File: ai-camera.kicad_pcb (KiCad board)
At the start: 4 copper layers, 70 x 70 mm, 188 parts, among them J1 Conn-01x02_P2mm_S2B-PH-K-S_Ho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, J2 USB_B_Micro_10118194-0001LF, J3 DBG, J4 Conn-02x10_P2.54mm_B-2100S20P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, J5 Conn-01x02_P1.25mm_10114829-1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, J6 Conn_01x24_FFC_0.5mm_hirose_F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, J7 Conn_01x24_FFC_0.5mm_hirose_F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, Q1 AO3401A, Q10 AO3401A, Q2 AO3400A, Q3 AO3400A, Q4 AO3400A, Q5 AO3401A, Q6 AO3400A, Q7 AO3401A, Q8 AO3400A, Q9 AO3400A, SW1 SW_PB_TS-1187A-B-A-B, SW2 SW_PB_TS-1187A-B-A-B, SW3 SW_PB_TS-1187A-B-A-B, SW4 SW_PB_TS-1187A-B-A-B, U1 SRV05-4, U10 RT9166-12GVL, U11 ESP32-S3-WROOM-1-N16R8, U12 MT9284-28J, U2 TP4057-42-SOT26-R, U3 PCF8563T/5,518, U4 XC6206-2.8V, U5 PIR_BS612, U6 SY8089AAAC, U7 SOT-23-6_SN74LVC1G373DBVR_TI, U8 AP1511B, U9 XC6206-2.8V, Y1 32.768kHz_Q13FC1350000400

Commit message: ai camera layout: begin
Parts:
- removed the C24 at (220.1, 92.6)
- removed the C29 at (230.4, 81.7)
- removed the Q4 at (247.4, 74.5)
- removed the R17 at (265.5, 72.6)
- removed the R20 at (265.9, 74.5)
- removed the R23 at (288.8, 51.1)
- removed the R24 at (259.5, 79.1)
- removed the R27 at (250.0, 88.3)
- removed the R34 at (273.3, 66.4)
- removed the R38 at (263.0, 77.5)
- removed the R39 at (279.3, 61.1)
- added C26: 1u_1206_CL31B105KCHNNNE, Capacitor_SMD:C_1206_3216Metric, F.Cu at (309.3, 32.7)
- added C28: 1u_1206_CL31B105KCHNNNE, Capacitor_SMD:C_1206_3216Metric, F.Cu at (315.1, 29.3)
- added C30: 100n_0402_CL05B104KB54PNC, Capacitor_SMD:C_0402_1005Metric, F.Cu at (307.9, 41.3)
- added C34: 1u_1206_CL31B105KCHNNNE, Capacitor_SMD:C_1206_3216Metric, F.Cu at (298.0, 36.0)
- added D5: B5819W-SL_SOD-123, Diode_SMD:D_SOD-123, F.Cu at (298.1, 29.3)
- added R18: 215k_0402_0402WGD2153TCE, Resistor_SMD:R_0402_1005Metric, F.Cu at (307.9, 39.3)
- added R21: 215k_0402_0402WGD2153TCE, Resistor_SMD:R_0402_1005Metric, F.Cu at (307.9, 35.4)
- added R25: 215k_0402_0402WGD2153TCE, Resistor_SMD:R_0402_1005Metric, F.Cu at (310.9, 38.0)
- added R32: 215k_0402_0402WGD2153TCE, Resistor_SMD:R_0402_1005Metric, F.Cu at (313.6, 34.0)
- added R33: 215k_0402_0402WGD2153TCE, Resistor_SMD:R_0402_1005Metric, F.Cu at (316.5, 32.0)
- added R36: 215k_0402_0402WGD2153TCE, Resistor_SMD:R_0402_1005Metric, F.Cu at (313.6, 32.0)
- C13, C19, C20, C21, C4, C6: value 22u_1206_CL31A226KOHNNNE -> 1u_1206_CL31B105KCHNNNE
- C27: value 100n_0402_CL05B104KB54PNC -> 22u_1206_CL31A226KOHNNNE; footprint Capacitor_SMD:C_0402_1005Metric -> Capacitor_SMD:C_1206_3216Metric
- R16, R19, R22, R37: value 10k_0402_0402WGF1002TCE -> 215k_0402_0402WGD2153TCE
- moved L1 174.6 mm to (102.3, 67.5)
- moved R6 172.4 mm to (171.9, 154.5)
- moved C3 170.4 mm to (101.2, 85.0), turned to 180 degrees
- moved R9 156.9 mm to (163.8, 129.5)
- moved R15 155.5 mm to (151.1, 131.2), turned to 90 degrees
- moved U2 139.7 mm to (160.7, 130.0)
- moved H3 133.6 mm to (279.8, 104.6)
- moved J4 133.6 mm to (269.2, 118.1)
- moved J5 133.6 mm to (282.0, 140.1)
- moved SW2 133.6 mm to (275.1, 145.6)
- moved H1 133.6 mm to (279.1, 162.2)
- moved J6 133.6 mm to (234.8, 137.0)
- moved J7 133.6 mm to (264.7, 102.5)
- moved L2 133.6 mm to (231.8, 156.5)
- moved L3 133.6 mm to (246.6, 156.5)
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- renumbered C16 to C15, C17 to C16, C15 to C17, C22 to C18, C23 to C22, C18 to C23, C25 to C24, C26 to C25, C28 to C29, C30 to C31, C31 to C32, C32 to C33, C33 to C35, C34 to C36, C35 to C37, C36 to C38, D5 to D6, D6 to D7, Q5 to Q4, Q6 to Q5, Q7 to Q6, Q8 to Q7, Q9 to Q8, Q10 to Q9, R3 to R1, R18 to R17, R4 to R2, R21 to R20, R25 to R23, R26 to R24, R28 to R26, R29 to R27, R30 to R28, R31 to R29, R5 to R3, R32 to R30, R33 to R31, R35 to R34, R36 to R35, R40 to R38, R41 to R39, R6 to R4, R42 to R40, R7 to R5, R1 to R6, R2 to R7
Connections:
- C18 pad 1: +3V3 -> GND
- C18 pad 2: GND -> +3V3
- C19 pad 1: Net-(C19-Pad1) -> GND
- C19 pad 2: GND -> +3V3
- C20 pad 1: Net-(C19-Pad1) -> Net-(Q9-Pad3)
- C21 pad 1: +3V3 -> Net-(Q9-Pad3)
- C22 pad 1: +3V3 -> GND
- C22 pad 2: GND -> +3V3
- C27 pad 1: +3V3 -> GND
- C27 pad 2: GND -> VBUS
- C4 pad 1: VBUS -> GND
- C4 pad 2: GND -> VBUS
- C6 pad 1: Net-(C6-Pad1) -> Net-(Q1-Pad1)
- C6 pad 2: Net-(C6-Pad2) -> Net-(Q1-Pad2)
- J4 pad 19: /IO40 -> GND
- JP1 pad 1: Net-(D1-Pad1) -> Net-(JP1-Pad1)
- JP1 pad 2: VBUS -> Net-(D1-Pad1)
- Q1 pad 1: Net-(C6-Pad2) -> Net-(Q1-Pad1)
- Q1 pad 2: Net-(C6-Pad1) -> Net-(Q1-Pad2)
- Q4 pad 1: Net-(C6-Pad2) -> Net-(Q1-Pad1)
- Q4 pad 2: Net-(C6-Pad1) -> Net-(Q1-Pad2)
- Q5 pad 3: Net-(Q6-Pad3) -> Net-(Q5-Pad3)
- Q6 pad 1: Net-(Q6-Pad3) -> Net-(Q5-Pad3)
- Q6 pad 3: Net-(Q7-Pad3) -> Net-(Q6-Pad3)
- Q7 pad 3: Net-(Q6-Pad3) -> Net-(Q5-Pad3)
- Q8 pad 1: /PWR_EN -> /CAM_PWR_EN
- Q9 pad 3: Net-(C19-Pad1) -> Net-(Q9-Pad3)
- R12 pad 1: Net-(C6-Pad2) -> Net-(Q1-Pad1)
- R12 pad 2: Net-(C6-Pad1) -> Net-(Q1-Pad2)
- R15 pad 1: Net-(Q4-Pad3) -> Net-(JP1-Pad1)
- R15 pad 2: Net-(C6-Pad2) -> Net-(Q1-Pad1)
- R16 pad 2: Net-(D1-Pad1) -> Net-(JP2-Pad2)
- R19 pad 1: Net-(Q6-Pad3) -> GND
- R19 pad 2: VBUS -> /PWR_EN
- R22 pad 2: Net-(Q7-Pad3) -> /PIR_CTRL_LE
- R37 pad 1: /IRCUT_CTRL -> /CAM.PWDN
- R6 pad 1: +5P -> Net-(D1-Pad1)
- SW1 pad 1: Net-(Q6-Pad3) -> Net-(Q5-Pad3)
- TP17 pad 1: /IO40 -> /CAM_PWR_EN
- U1 pad 5: +5F -> Net-(J2-Pad1)
- U10 pad 3: Net-(C19-Pad1) -> Net-(Q9-Pad3)
- U11 pad 33: /IO40 -> /CAM_PWR_EN
- U3 pad 3: Net-(Q6-Pad3) -> Net-(Q5-Pad3)
- U6 pad 1: Net-(Q7-Pad3) -> Net-(Q6-Pad3)
- U9 pad 3: Net-(C19-Pad1) -> Net-(Q9-Pad3)

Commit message: ai camera review 8: replace 1u/1206 with 10u/0603
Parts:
- removed the C17 at (214.4, 92.6)
- removed Q8: AO3400A, Package_TO_SOT_SMD:SOT-23
- removed Q9: AO3401A, Package_TO_SOT_SMD:SOT-23
- removed the R15 at (151.1, 131.2)
- removed the R33 at (316.5, 32.0)
- removed the R34 at (295.1, 46.0)
- removed the R35 at (280.3, 59.1)
- removed R37: 215k_0402_0402WGD2153TCE, Resistor_SMD:R_0402_1005Metric
- removed the TP10 at (255.1, 73.5)
- removed the TP11 at (234.8, 90.7)
- removed the TP12 at (292.1, 42.8)
- removed the TP9 at (229.5, 96.9)
- added C1: 1u_1206_CL31B105KCHNNNE, Capacitor_SMD:C_1206_3216Metric, F.Cu at (238.5, 90.5)
- added C8: 100n_0402_CL05B104KB54PNC, Capacitor_SMD:C_0402_1005Metric, F.Cu at (242.8, 91.8)
- added R12: 215k_0402_0402WGD2153TCE, Resistor_SMD:R_0402_1005Metric, F.Cu at (242.8, 89.8)
- moved L1 89.6 mm to (110.3, 156.7)
- moved C4 89.6 mm to (109.2, 174.2)
- moved D1 89.6 mm to (118.8, 168.8)
- moved J1 89.6 mm to (109.7, 168.5)
- moved U1 89.6 mm to (110.1, 160.0)
- moved D2 89.6 mm to (121.1, 168.8)
- moved J2 89.6 mm to (105.7, 160.2)
- moved TP30 78.7 mm to (319.6, 100.8)
- moved TP49 75.9 mm to (313.0, 101.6)
- moved R18 74.8 mm to (225.2, 50.4)
- moved C16 74.8 mm to (224.0, 54.4)
- moved C21 74.8 mm to (228.1, 50.4)
- moved C39 74.8 mm to (224.0, 52.4)
- moved R14 74.8 mm to (228.1, 48.4)
- moved R32 74.5 mm to (239.4, 40.9)
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- renumbered C8 to C10, C9 to C11, C10 to C12, C11 to C13, C12 to C14, C13 to C15, C14 to C16, C15 to C17, C16 to C18, C20 to C19, C1 to C2, C21 to C20, C18 to C21, C19 to C22, C24 to C23, C25 to C24, C22 to C25, C23 to C26, C26 to C27, C27 to C28, C28 to C29, C2 to C3, C29 to C30, C30 to C31, C31 to C32, C32 to C33, C33 to C34, C34 to C35, C35 to C36, C36 to C37, C37 to C38, C38 to C39, C3 to C4, C4 to C5, C5 to C7, C7 to C9, R12 to R15, R18 to R17, R17 to R18, R21 to R20, R20 to R21, R23 to R22, R24 to R23, R22 to R24, R36 to R33, R38 to R34, R39 to R35, R40 to R36, TP14 to TP10, TP15 to TP11, TP16 to TP12, TP17 to TP13, TP18 to TP14, TP19 to TP15, TP20 to TP16, TP21 to TP17, TP22 to TP18, TP23 to TP19, TP24 to TP20, TP25 to TP21, TP26 to TP22, TP27 to TP23, TP28 to TP24, TP29 to TP25, TP30 to TP26, TP31 to TP27, TP32 to TP28, TP33 to TP29, TP34 to TP30, TP35 to TP31, TP36 to TP32, TP37 to TP33, TP38 to TP34, TP39 to TP35, TP40 to TP36, TP41 to TP37, TP42 to TP38, TP43 to TP39, TP44 to TP40, TP45 to TP41, TP46 to TP42, TP47 to TP43, TP48 to TP44, TP49 to TP45, TP50 to TP46, TP51 to TP47, TP52 to TP48, TP53 to TP49, TP54 to TP50, TP55 to TP51, TP56 to TP52, TP57 to TP53, TP58 to TP54, TP59 to TP55, TP13 to TP9, U8 to U10, U9 to U8, U10 to U9
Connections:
- C19 pad 1: Net-(Q9-Pad3) -> +3V3
- C20 pad 1: Net-(Q9-Pad3) -> +3V3
- C6 pad 1: Net-(Q1-Pad1) -> Net-(C6-Pad1)
- C6 pad 2: Net-(Q1-Pad2) -> Net-(C6-Pad2)
- D5 pad 2: Net-(JP1-Pad1) -> Net-(D5-Pad2)
- J4 pad 11: /IO36 -> /SDA
- J4 pad 13: /IO37 -> /SCL
- JP1 pad 1: Net-(JP1-Pad1) -> Net-(D5-Pad2)
- Q1 pad 1: Net-(Q1-Pad1) -> Net-(C6-Pad1)
- Q1 pad 2: Net-(Q1-Pad2) -> Net-(C6-Pad2)
- Q4 pad 1: Net-(Q1-Pad1) -> Net-(C6-Pad1)
- Q4 pad 2: Net-(Q1-Pad2) -> Net-(C6-Pad2)
- R15 pad 1: Net-(Q1-Pad1) -> Net-(D5-Pad2)
- R15 pad 2: Net-(Q1-Pad2) -> Net-(C6-Pad1)
- U11 pad 15: /CAM.D9 -> /CAM.SCL
- U11 pad 16: /CAM.HREF -> /IRLED_PWM
- U11 pad 20: /CAM.SCL -> /CAM.D9
- U11 pad 28: /IRLED_PWM -> unconnected-(U11-Pad28)
- U11 pad 29: /IO36 -> unconnected-(U11-Pad29)
- U11 pad 30: /IO37 -> unconnected-(U11-Pad30)
- U11 pad 33: /CAM_PWR_EN -> /CAM.HREF
- U8 pad 3: Net-(Q9-Pad3) -> +3V3
- U9 pad 3: Net-(Q9-Pad3) -> +3V3

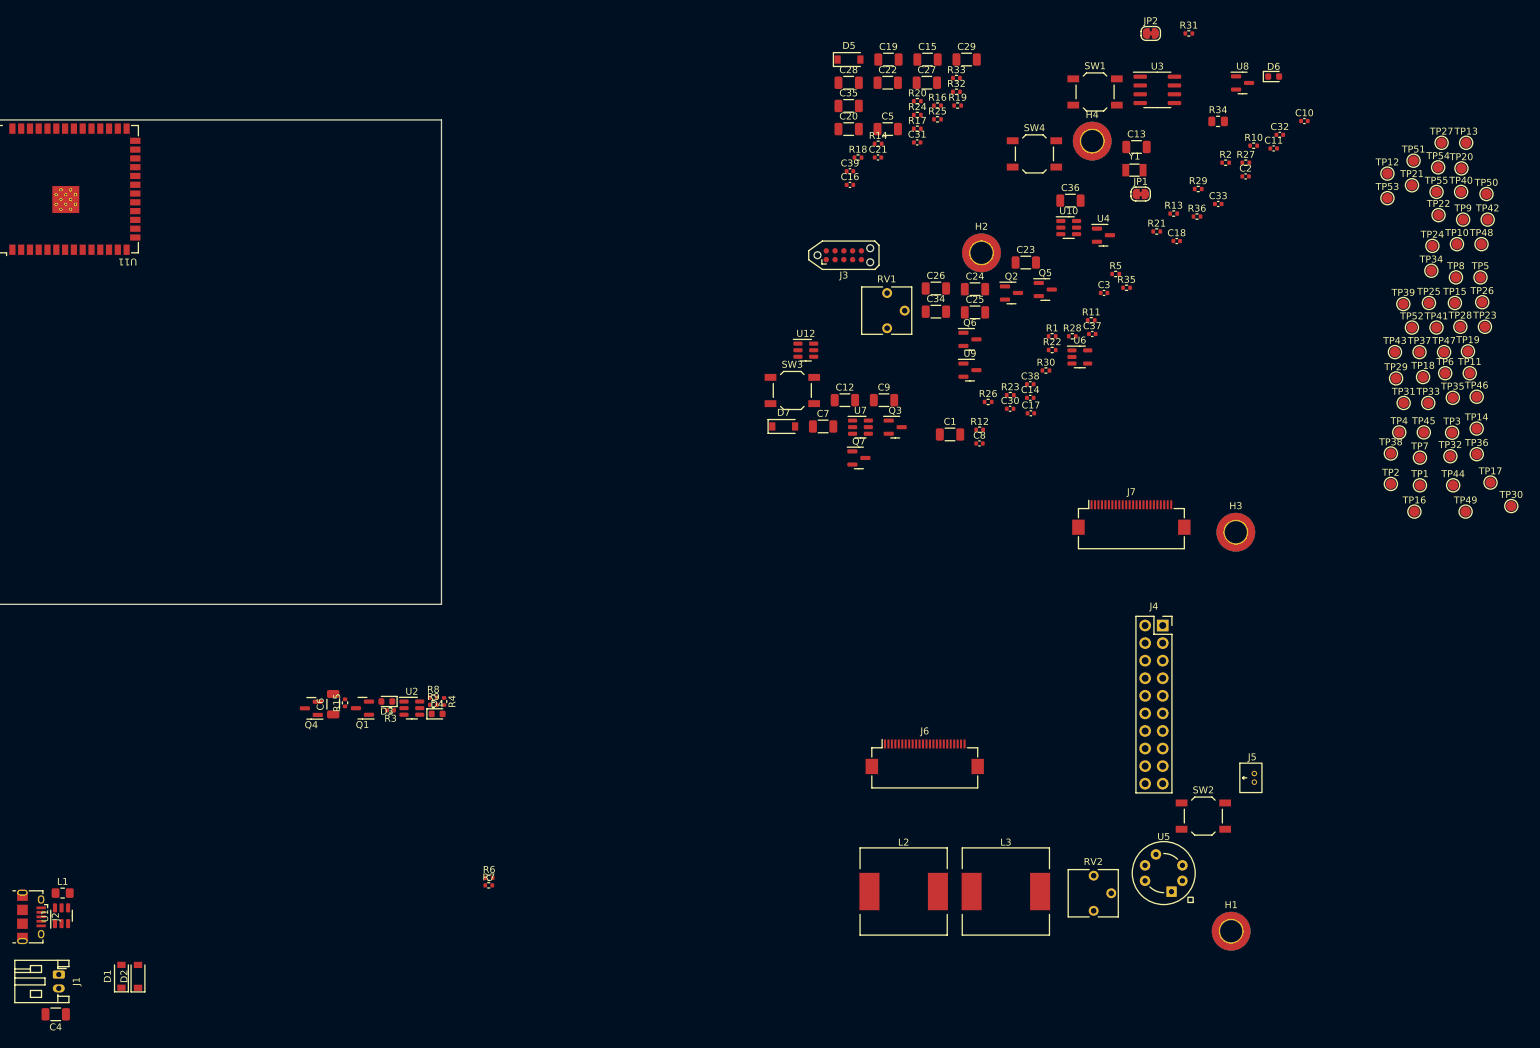
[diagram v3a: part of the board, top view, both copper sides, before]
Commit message: ai camera review 9: replace replace 1u/1206 with 10u/0603
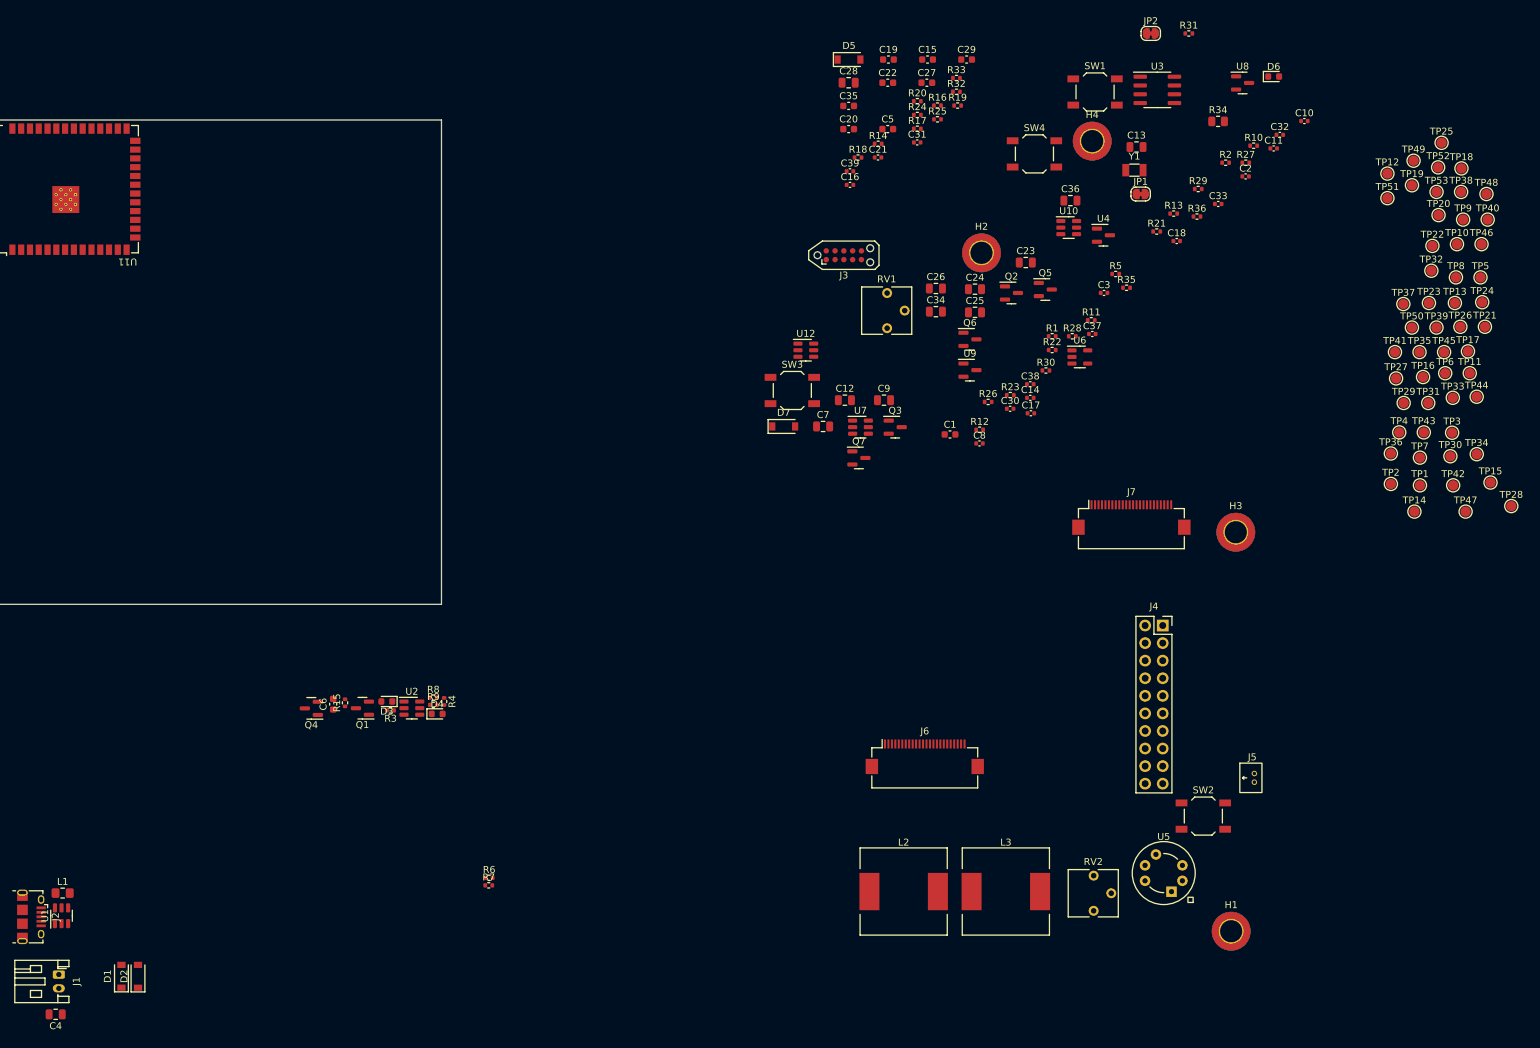
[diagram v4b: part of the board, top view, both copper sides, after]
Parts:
- removed the TP13 at (313.1, 48.3)
- removed the TP14 at (314.6, 89.6)
- C1, C15, C19, C20, C22, C27, C29, C35, C5, C6: value 1u_1206_CL31B105KCHNNNE -> 10u_0603_CL10A106KP8NNNC; footprint Capacitor_SMD:C_1206_3216Metric -> Capacitor_SMD:C_0603_1608Metric
- C12, C13, C23, C24, C25, C26, C28, C34, C36, C4, C7, C9: value 22u_1206_CL31A226KOHNNNE -> 22u_0805_CL21A226MAQNNNE; footprint Capacitor_SMD:C_1206_3216Metric -> Capacitor_SMD:C_0805_2012Metric
- renumbered TP15 to TP13, TP16 to TP14, TP17 to TP15, TP18 to TP16, TP19 to TP17, TP20 to TP18, TP21 to TP19, TP22 to TP20, TP23 to TP21, TP24 to TP22, TP25 to TP23, TP26 to TP24, TP27 to TP25, TP28 to TP26, TP29 to TP27, TP30 to TP28, TP31 to TP29, TP32 to TP30, TP33 to TP31, TP34 to TP32, TP35 to TP33, TP36 to TP34, TP37 to TP35, TP38 to TP36, TP39 to TP37, TP40 to TP38, TP41 to TP39, TP42 to TP40, TP43 to TP41, TP44 to TP42, TP45 to TP43, TP46 to TP44, TP47 to TP45, TP48 to TP46, TP49 to TP47, TP50 to TP48, TP51 to TP49, TP52 to TP50, TP53 to TP51, TP54 to TP52, TP55 to TP53

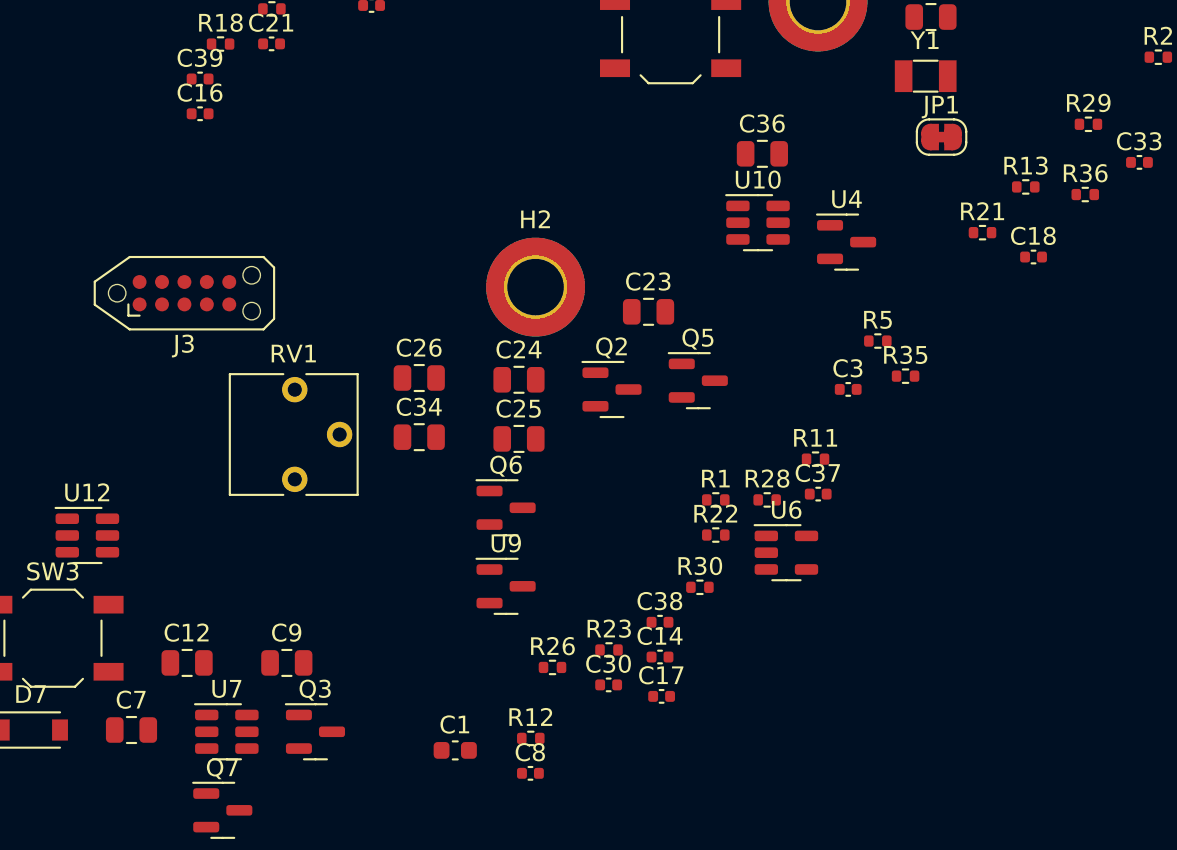
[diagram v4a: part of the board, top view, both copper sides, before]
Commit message: ai camera review 10: replace some 22u with 10u to save the board space
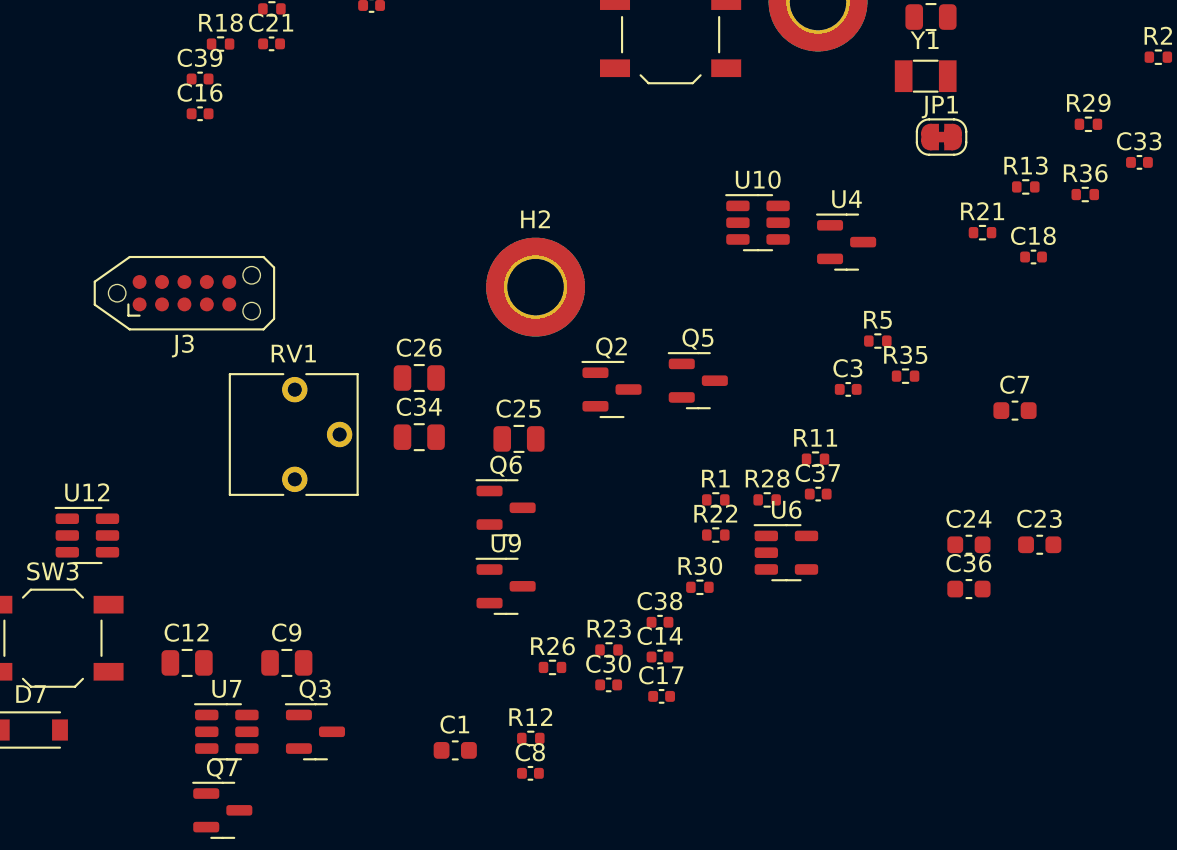
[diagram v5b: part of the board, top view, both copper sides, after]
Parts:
- C23, C24, C36, C7: value 22u_0805_CL21A226MAQNNNE -> 10u_0603_CL10A106KP8NNNC; footprint Capacitor_SMD:C_0805_2012Metric -> Capacitor_SMD:C_0603_1608Metric
- moved C7 53.2 mm to (270.2, 71.2)
- moved C36 27.3 mm to (267.6, 81.3)
- moved C24 27.1 mm to (267.6, 78.8)
- moved C23 25.8 mm to (271.6, 78.8)
